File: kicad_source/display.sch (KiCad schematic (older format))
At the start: 19 parts, among them CN3 CONN_01X24, Q1 SI1304BDL

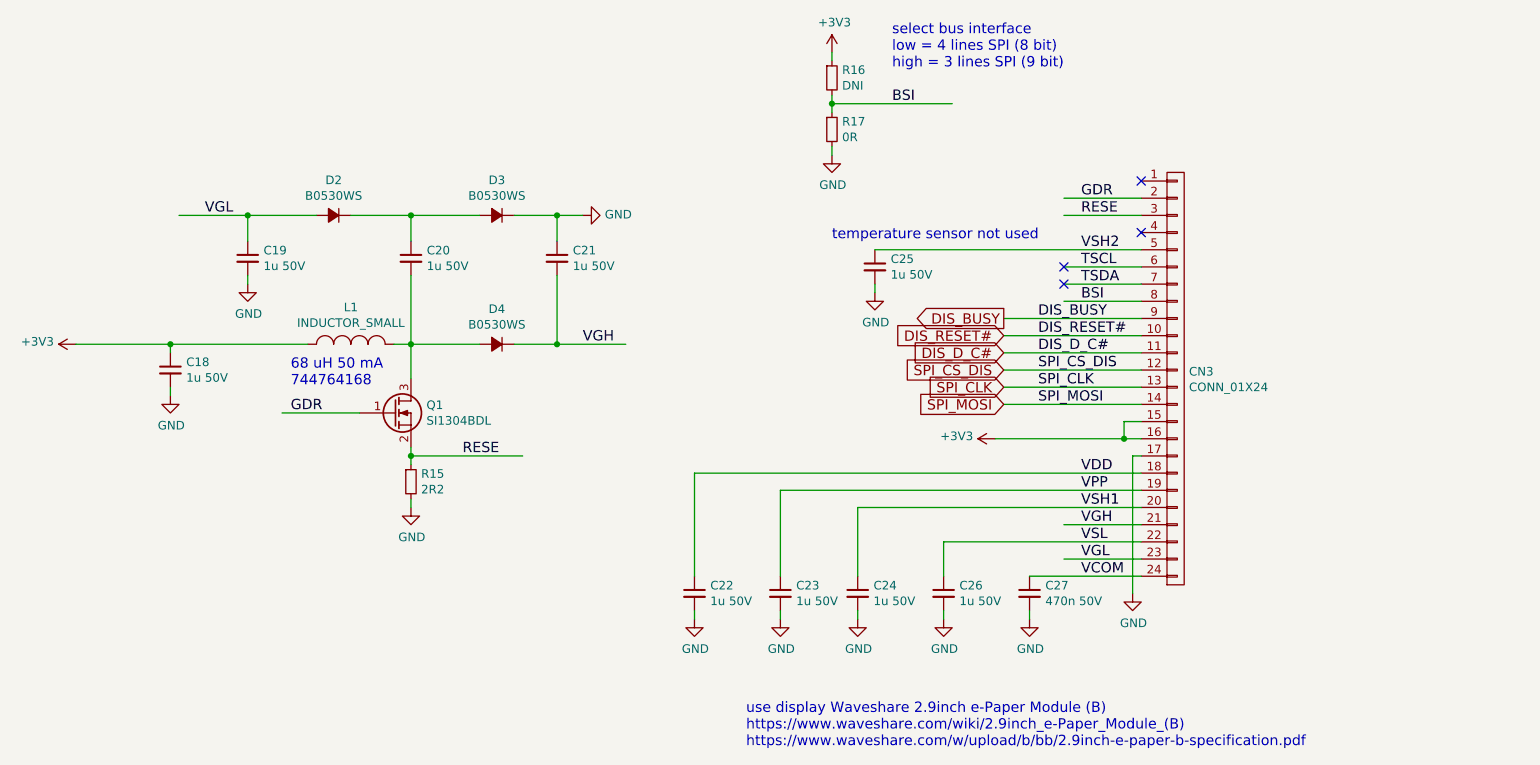
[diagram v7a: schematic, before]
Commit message: corrected some part numbers
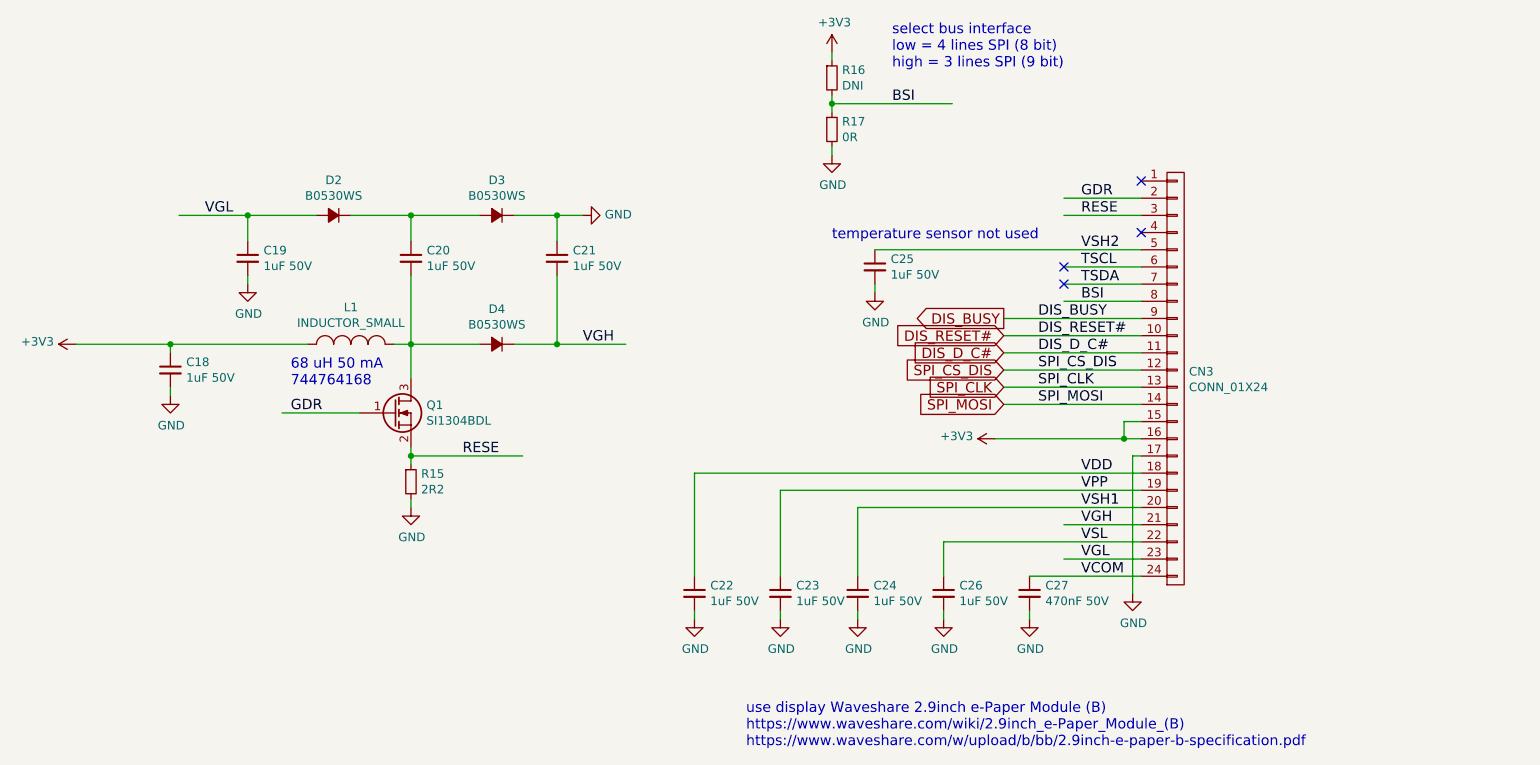
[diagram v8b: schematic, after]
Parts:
- C18, C19, C20, C21, C22, C23, C24, C25, C26: value 1u 50V -> 1uF 50V
- C27: value 470n 50V -> 470nF 50V
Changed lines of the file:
@@
 P 7050 2900
 F 0 "C25" H 7142 2946 50  0000 L CNN
-F 1 "1u 50V" H 7142 2855 50  0000 L CNN
+F 1 "1uF 50V" H 7142 2855 50  0000 L CNN
 F 2 "capacitors:C_0603" H 7050 2750 50  0001 C CNN
 F 3 "" H 7050 2900 50  0000 C CNN
@@
 P 7950 4800
 F 0 "C27" H 8042 4846 50  0000 L CNN
-F 1 "470n 50V" H 8042 4755 50  0000 L CNN
+F 1 "470nF 50V" H 8042 4755 50  0000 L CNN
 F 2 "capacitors:C_0603" H 7950 4650 50  0001 C CNN
 F 3 "" H 7950 4800 50  0000 C CNN
@@
 P 7450 4800
 F 0 "C26" H 7542 4846 50  0000 L CNN
-F 1 "1u 50V" H 7542 4755 50  0000 L CNN
+F 1 "1uF 50V" H 7542 4755 50  0000 L CNN
 F 2 "capacitors:C_0603" H 7450 4650 50  0001 C CNN
 F 3 "" H 7450 4800 50  0000 C CNN
@@
 P 6950 4800
 F 0 "C24" H 7042 4846 50  0000 L CNN
-F 1 "1u 50V" H 7042 4755 50  0000 L CNN
+F 1 "1uF 50V" H 7042 4755 50  0000 L CNN
 F 2 "capacitors:C_0603" H 6950 4650 50  0001 C CNN
 F 3 "" H 6950 4800 50  0000 C CNN
@@
 P 6500 4800
 F 0 "C23" H 6592 4846 50  0000 L CNN
-F 1 "1u 50V" H 6592 4755 50  0000 L CNN
+F 1 "1uF 50V" H 6592 4755 50  0000 L CNN
 F 2 "capacitors:C_0603" H 6500 4650 50  0001 C CNN
 F 3 "" H 6500 4800 50  0000 C CNN
@@
 P 6000 4800
 F 0 "C22" H 6092 4846 50  0000 L CNN
-F 1 "1u 50V" H 6092 4755 50  0000 L CNN
+F 1 "1uF 50V" H 6092 4755 50  0000 L CNN
 F 2 "capacitors:C_0603" H 6000 4650 50  0001 C CNN
 F 3 "" H 6000 4800 50  0000 C CNN
@@
 P 4350 2850
 F 0 "C20" H 4442 2896 50  0000 L CNN
-F 1 "1u 50V" H 4442 2805 50  0000 L CNN
+F 1 "1uF 50V" H 4442 2805 50  0000 L CNN
 F 2 "capacitors:C_0603" H 4350 2700 50  0001 C CNN
 F 3 "" H 4350 2850 50  0000 C CNN
@@
 P 5200 2850
 F 0 "C21" H 5292 2896 50  0000 L CNN
-F 1 "1u 50V" H 5292 2805 50  0000 L CNN
+F 1 "1uF 50V" H 5292 2805 50  0000 L CNN
 F 2 "capacitors:C_0603" H 5200 2700 50  0001 C CNN
 F 3 "" H 5200 2850 50  0000 C CNN
@@
 P 3400 2850
 F 0 "C19" H 3492 2896 50  0000 L CNN
-F 1 "1u 50V" H 3492 2805 50  0000 L CNN
+F 1 "1uF 50V" H 3492 2805 50  0000 L CNN
 F 2 "capacitors:C_0603" H 3400 2700 50  0001 C CNN
 F 3 "" H 3400 2850 50  0000 C CNN
@@
 P 2950 3500
 F 0 "C18" H 3042 3546 50  0000 L CNN
-F 1 "1u 50V" H 3042 3455 50  0000 L CNN
+F 1 "1uF 50V" H 3042 3455 50  0000 L CNN
 F 2 "capacitors:C_0603" H 2950 3350 50  0001 C CNN
 F 3 "" H 2950 3500 50  0000 C CNN
